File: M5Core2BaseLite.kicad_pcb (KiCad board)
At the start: 2 copper layers, 50 x 50 mm, 68 parts, among them CN1 CON_GROVEH, CN2 CON_GROVEH, CN3 CON_GROVEH, CN4 CON_GROVEH, CN5 CON_GROVEV, CN6 MBUS_bottom, CN7 PinHeader_2x15_P2.54mm_Vertic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, CN8 CON_GROVEH, CN9 CON_GROVEH, J1 Conn_01x02_Female, J2 Conn_01x02_Female, J3 Conn_01x08_Female, U1 LED_SK6812side, U10 LED_SK6812side, U2 LED_SK6812side, U3 LED_SK6812side, U4 LED_SK6812side, U5 LED_SK6812side, U6 LED_SK6812side, U7 LED_SK6812side, U8 LED_SK6812side, U9 LED_SK6812side

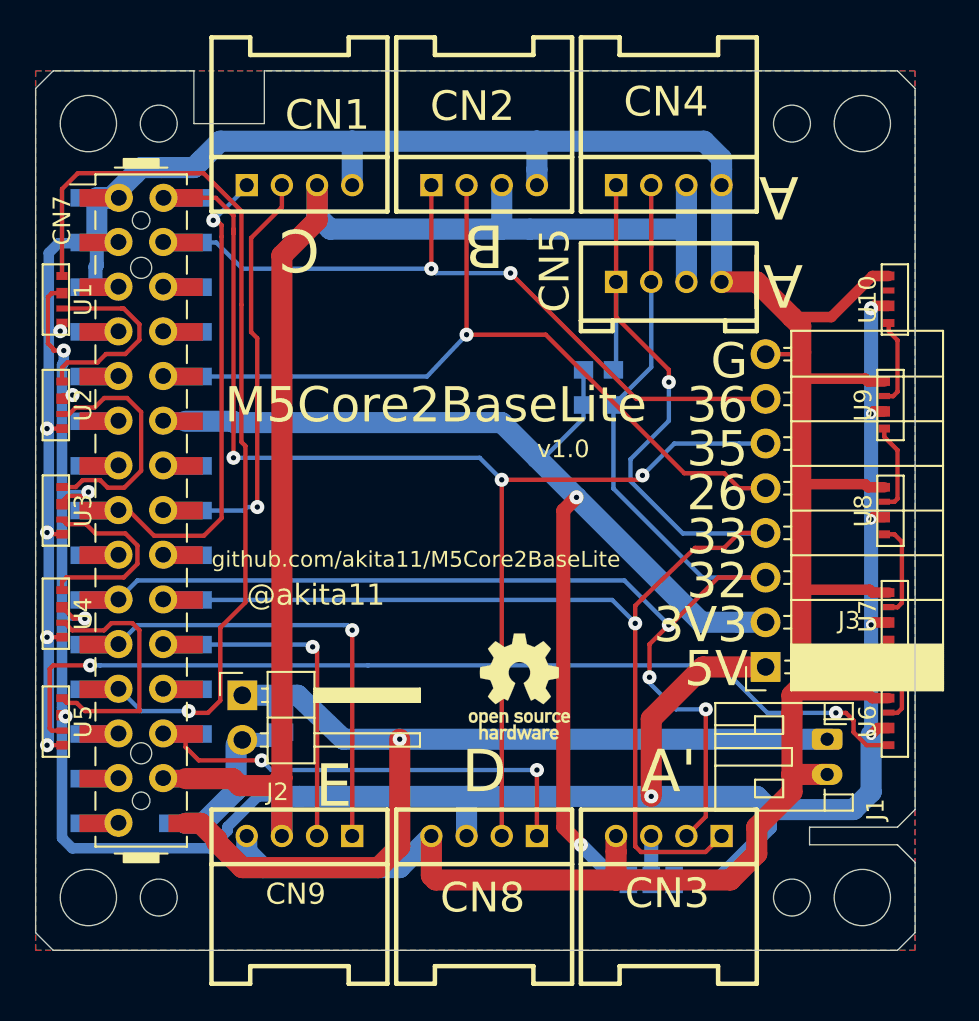
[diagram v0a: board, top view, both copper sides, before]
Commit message: 基板データをv1.0a（PortA'をデフォルト5V）に変更
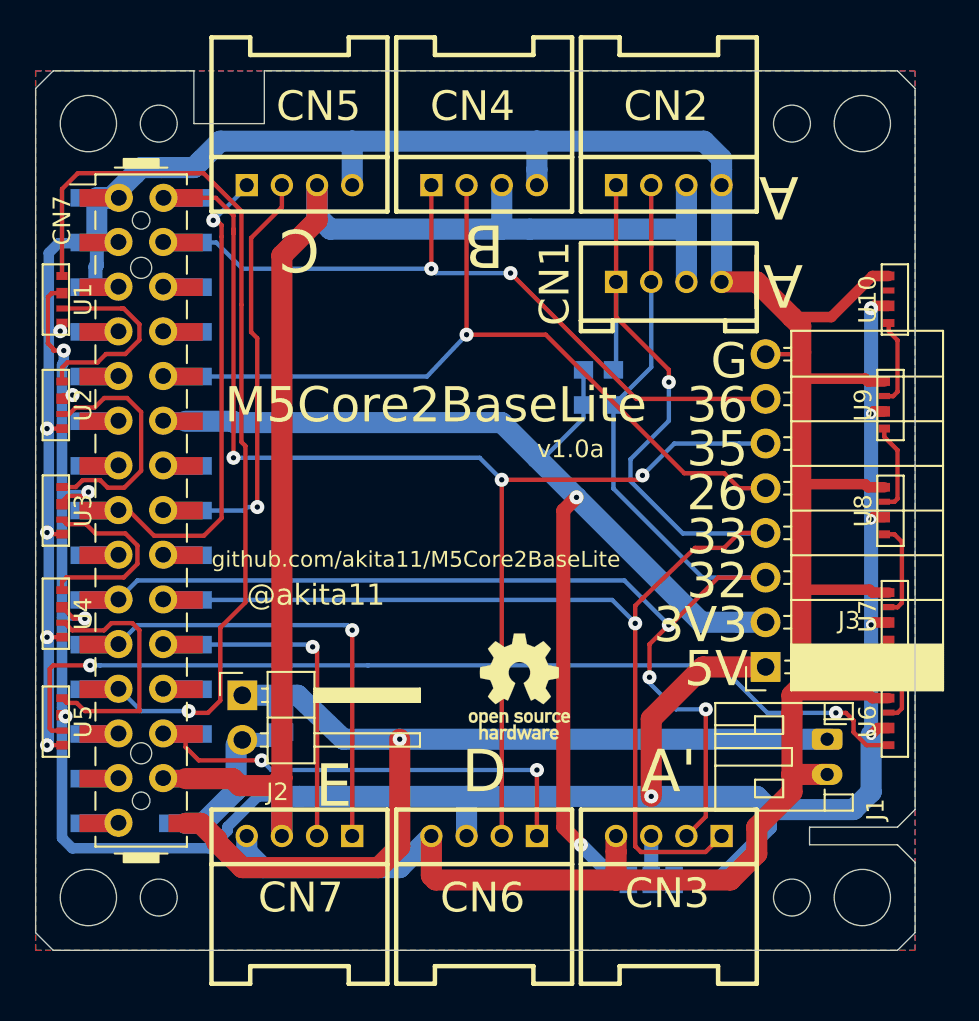
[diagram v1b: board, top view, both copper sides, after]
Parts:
- turned JP2 to 180 degrees
- renumbered CN5 to CN1, CN4 to CN2, CN2 to CN4, CN1 to CN5, CN8 to CN6, CN9 to CN7, CN6 to CN8
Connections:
- CN8 pad 11: Net-(CN6-Pad11) -> Net-(CN8-Pad11)
- CN8 pad 13: Net-(CN6-Pad13) -> Net-(CN8-Pad13)
- CN8 pad 14: Net-(CN6-Pad14) -> Net-(CN8-Pad14)
- CN8 pad 24: Net-(CN6-Pad24) -> Net-(CN8-Pad24)
- CN8 pad 25: Net-(CN6-Pad25) -> Net-(CN8-Pad25)
- CN8 pad 27: Net-(CN6-Pad27) -> Net-(CN8-Pad27)
- CN8 pad 29: Net-(CN6-Pad29) -> Net-(CN8-Pad29)
- CN8 pad 6: Net-(CN6-Pad6) -> Net-(CN8-Pad6)
- CN8 pad 7: Net-(CN6-Pad7) -> Net-(CN8-Pad7)
- CN8 pad 8: Net-(CN6-Pad8) -> Net-(CN8-Pad8)
- CN8 pad 9: Net-(CN6-Pad9) -> Net-(CN8-Pad9)
- JP2 pad 1: +3V3 -> +5V
- JP2 pad 3: +5V -> +3V3
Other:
- board text added: "v1.0a"
- board text removed: "v1.0"
